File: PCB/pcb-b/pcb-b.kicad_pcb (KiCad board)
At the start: 2 copper layers, 94.7 x 42 mm, 81 parts, among them J1 Conn_02x05_Counter_Clockwise, J2 Conn_02x05_Counter_Clockwise, K1 HK19F-DCxxV-SHC, Q1 BC817, Q10 BC817, Q11 TPCA8120,L1Q, Q13 TPCA8120,L1Q, Q14 BC817, Q15 BC817, Q19 BC817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

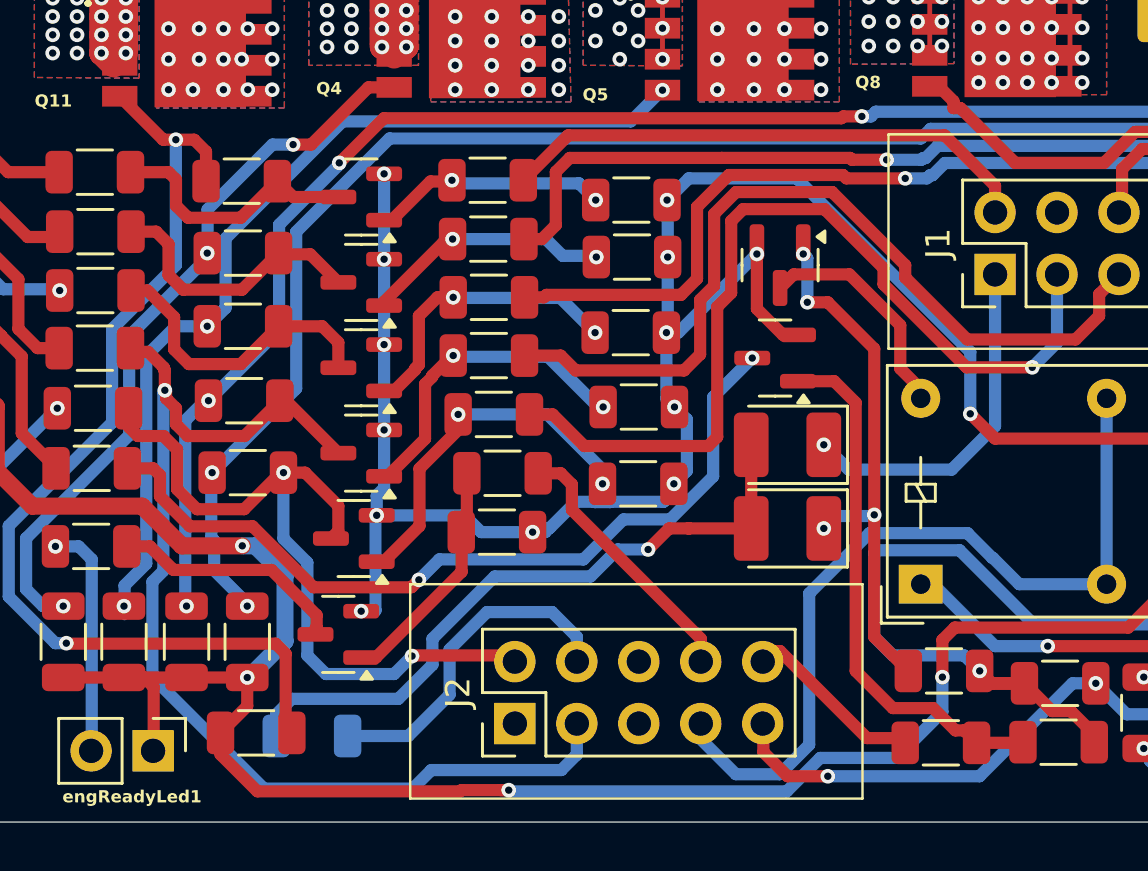
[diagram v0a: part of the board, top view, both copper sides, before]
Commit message: Small enhancement: all components on the same side
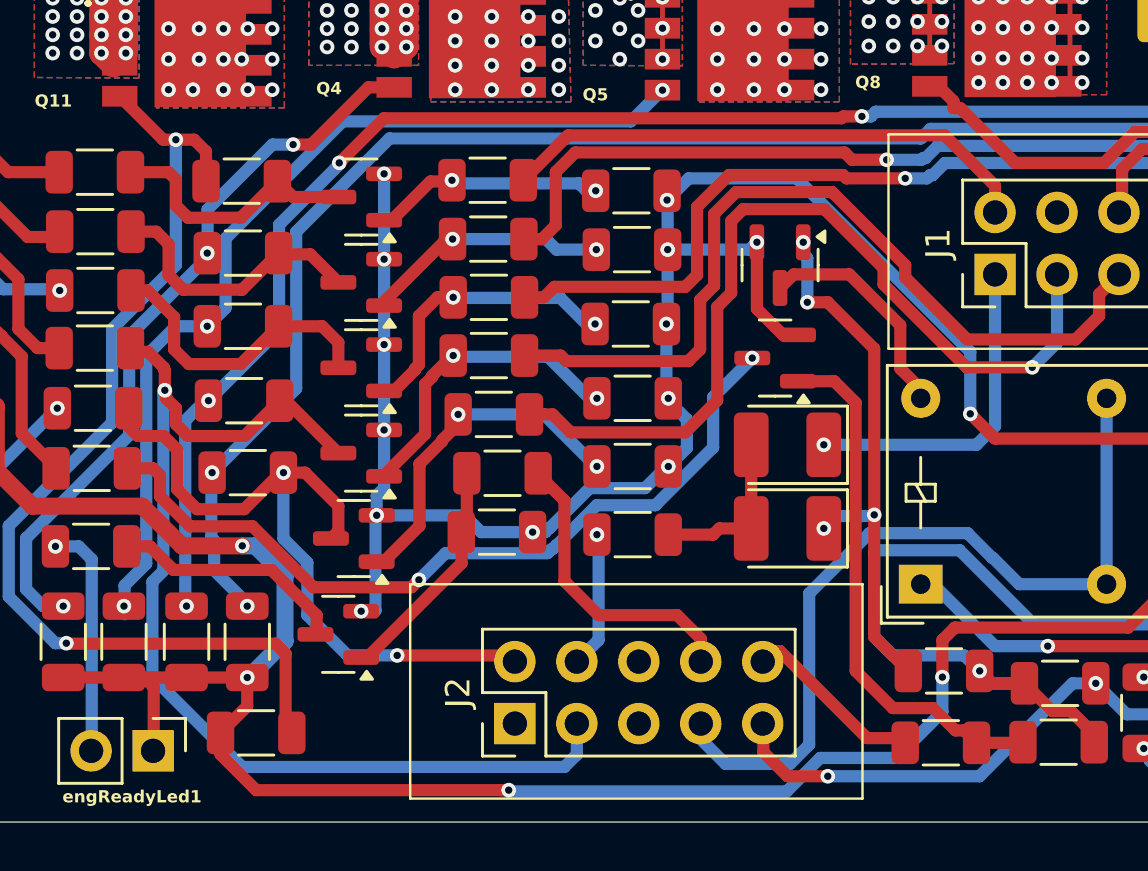
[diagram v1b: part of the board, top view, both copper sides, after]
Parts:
- RA15: moved to F.Cu
- moved RA15 15.5 mm to (137.7, 100.1), turned to 0 degrees
- moved RA38 0.75 mm to (137.7, 97.3)
- moved RA37 0.44 mm to (137.7, 94.5)
- moved RA34 0.38 mm to (137.6, 86.0)
- moved RA36 0.36 mm to (137.6, 91.5)
- moved RA35 0.30 mm to (137.7, 88.4)
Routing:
- net Net-(D2-A): track 27.6 -> 6.93 mm, vias 1 -> 0
- net o_engineON: track 14.7 -> 6.26 mm, vias 0 -> 1
- net GND: track 240.7 -> 238.8 mm
- net c_rightArrow: track 31.5 -> 29.9 mm
- net o_engineReady: track 11.0 -> 12.4 mm
- net o_rightArrow: track 37.3 -> 36.0 mm
- net Net-(Q19-B): track 15.0 -> 14.2 mm
- net i_powerOFF: track 14.4 -> 13.6 mm
- net c_leftArrow: track 45.7 -> 45.0 mm
- net Net-(Q20-C): track 33.9 -> 33.2 mm

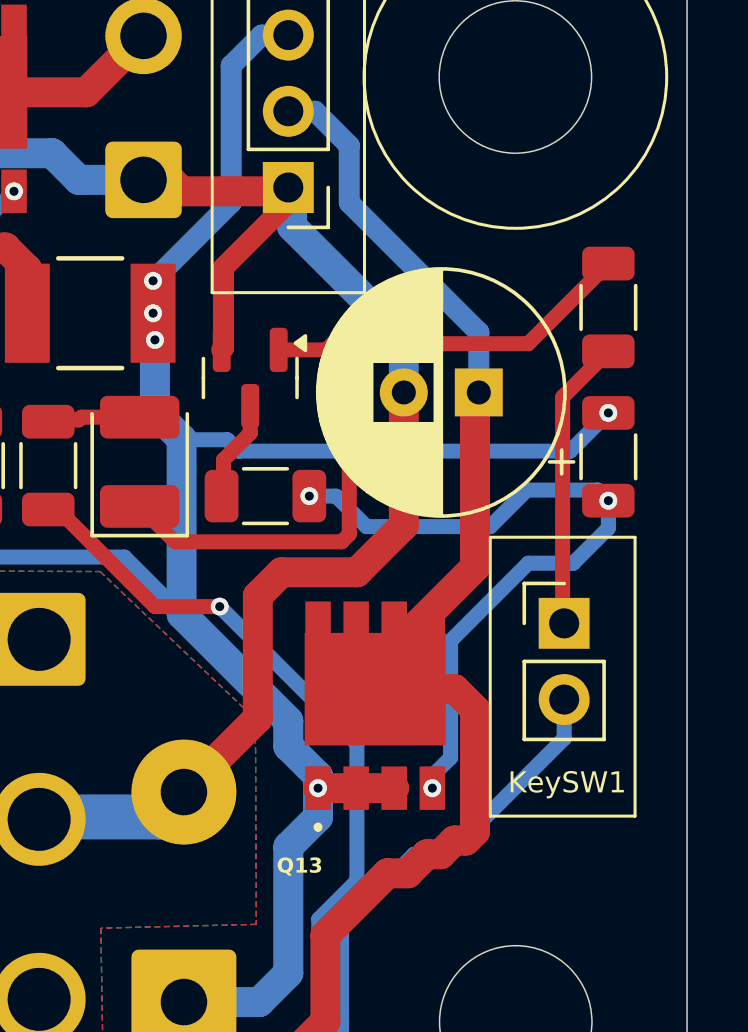
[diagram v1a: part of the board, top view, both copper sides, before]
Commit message: Floating BC817's base fixed
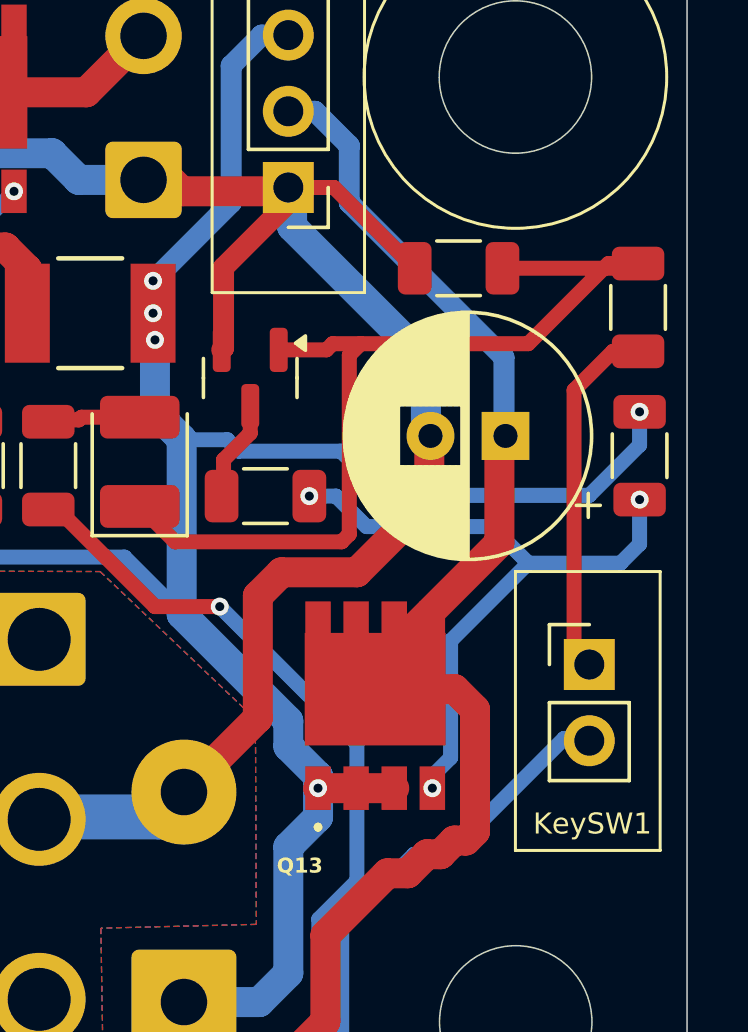
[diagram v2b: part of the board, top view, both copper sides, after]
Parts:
- added R7: 100K, Resistor_SMD:R_1206_3216Metric, F.Cu at (189.5, 81.6)
- moved C9 1.70 mm to (191.0, 87.2)
- moved KeySW1 1.61 mm to (193.8, 94.8)
- moved R2 1.04 mm to (195.5, 87.8)
- moved R4 0.99 mm to (195.4, 82.9)
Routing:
- net GND: track 238.8 -> 244.9 mm
- net Net-(D1-K): track 26.3 -> 31.7 mm
- net +12V: track 184.3 -> 187.3 mm
- net Net-(KeySW1-Pin_1): track 9.72 -> 12.0 mm
- net Net-(Q13-G): track 23.9 -> 22.5 mm
- net tempPower: track 115.9 -> 116.5 mm

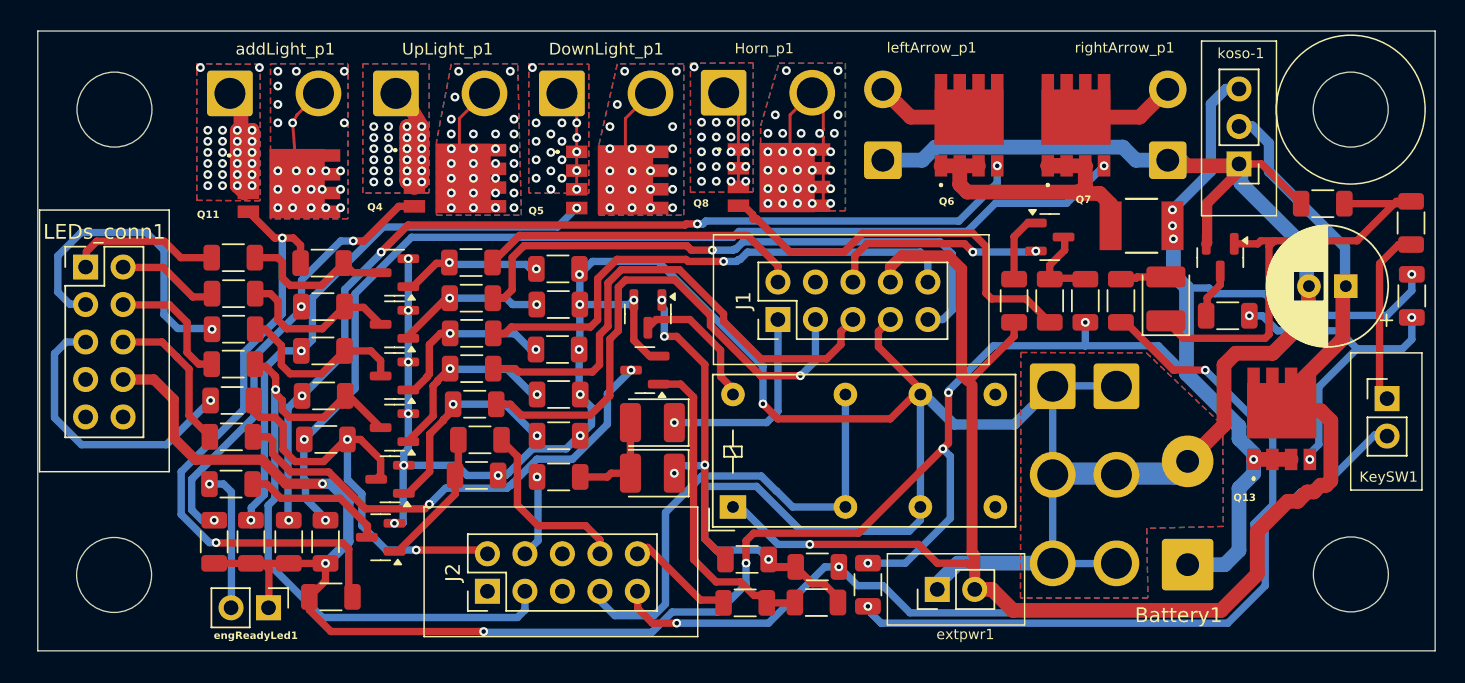
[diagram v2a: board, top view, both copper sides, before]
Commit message: Components sizes and positions optimizing
- 3-pins Koso's comnnector has been substituted with a more standard 4-pins one
- One resistor has been moved to free space for EngReady_led connector
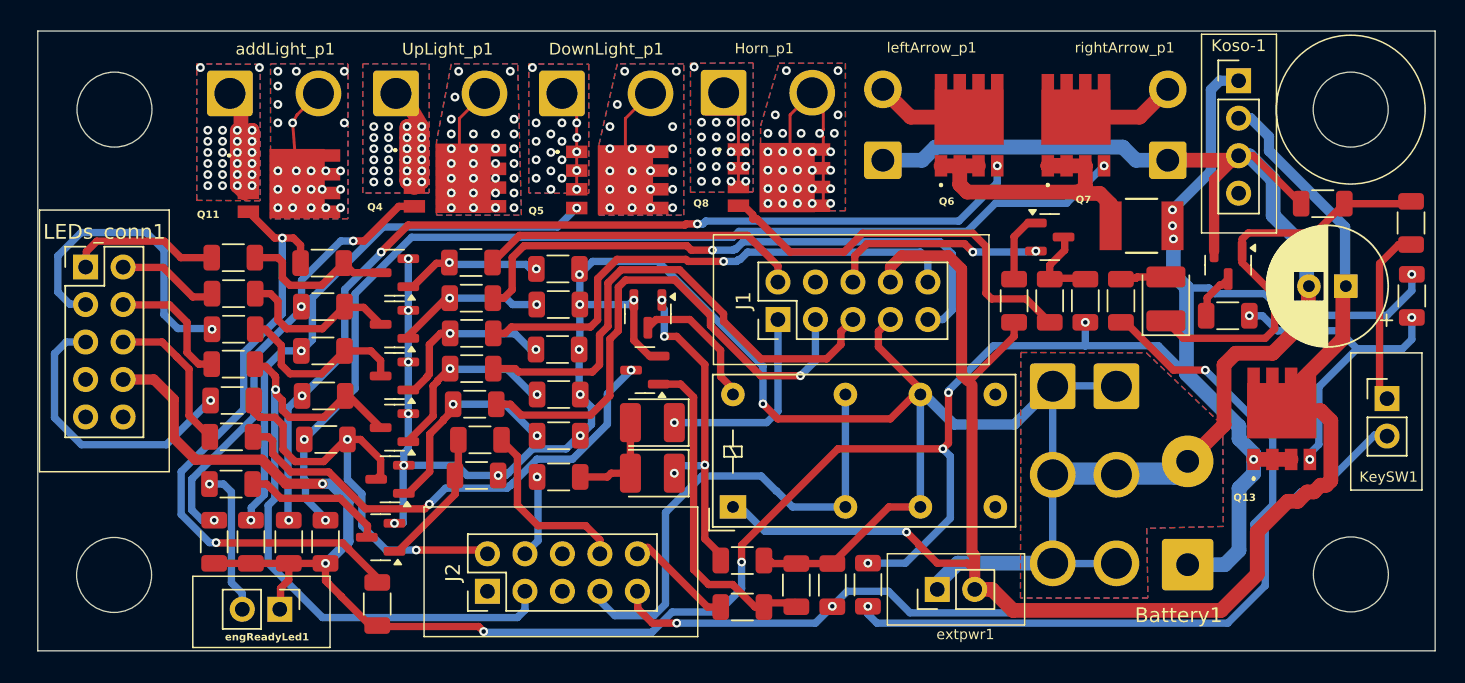
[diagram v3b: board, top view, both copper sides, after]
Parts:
- Koso-1: renamed from koso-1; value Conn_01x03 -> Conn_01x04; footprint Connector_PinHeader_2.54mm:PinHeader_1x03_P2.54mm_Vertical -> Connector_PinHeader_2.54mm:PinHeader_1x04_P2.54mm_Vertical
- moved Koso-1 5.64 mm to (183.8, 73.2), turned to 0 degrees
- moved RA24 3.18 mm to (125.4, 108.7), turned to 90 degrees
- moved RA39 1.80 mm to (153.8, 107.4), turned to 90 degrees
- moved R6 1.60 mm to (156.2, 107.4), turned to -90 degrees
- moved engReadyLed1 0.77 mm to (118.8, 109.1)
- moved Q9 0.74 mm to (183.0, 85.7)
- moved RA17 0.34 mm to (150.1, 108.9)
- moved RA8 0.33 mm to (150.1, 105.8)
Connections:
- Koso-1 pad 1: GND -> +12V
- Koso-1 pad 3: +12V -> GND
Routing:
- net GND: track 244.9 -> 226.1 mm, vias 15 -> 14
- net Net-(D1-K): track 31.7 -> 27.7 mm
- net +12V: track 187.3 -> 184.3 mm
- net o_keepAlive: track 71.7 -> 70.3 mm
- net Net-(Q20-B): track 21.8 -> 22.6 mm
- net tempPower: track 116.5 -> 117.1 mm

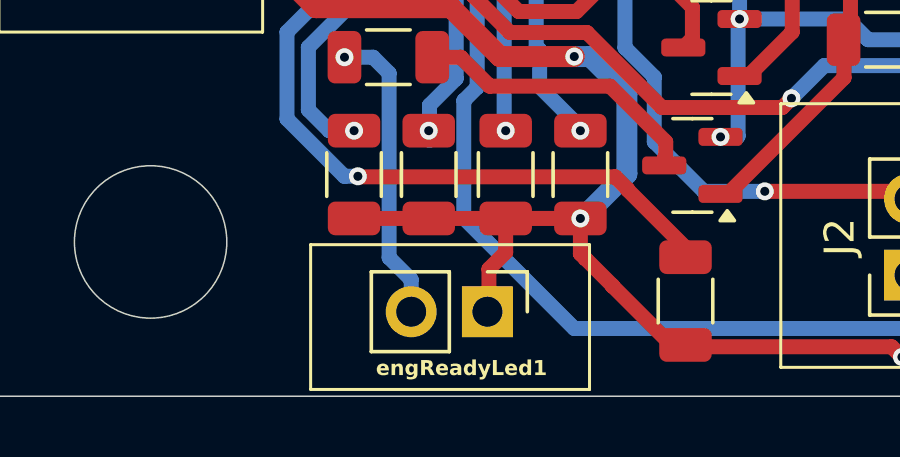
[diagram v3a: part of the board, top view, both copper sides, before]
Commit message: Wrong EngReady_LED connector orientation fixed
Standard: 1=negative 2=positive
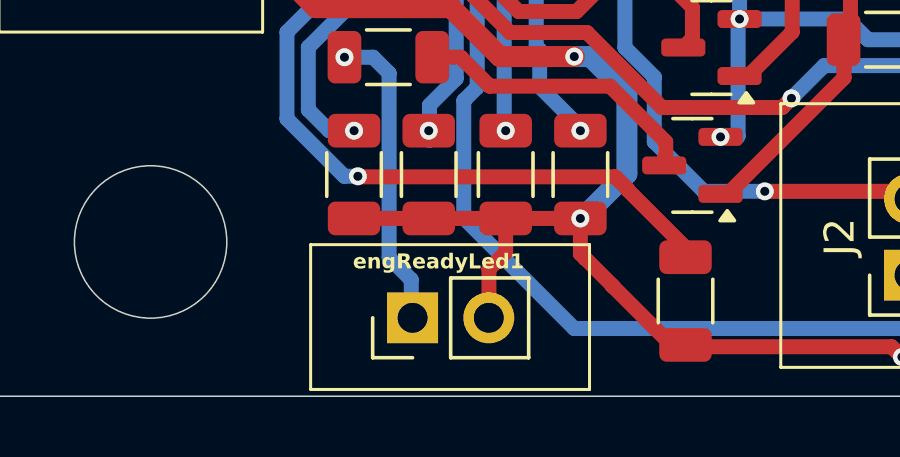
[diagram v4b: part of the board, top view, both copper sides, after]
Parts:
- moved engReadyLed1 2.50 mm to (116.3, 109.3), turned to 90 degrees
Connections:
- RA9 pad 2: Net-(engReadyLed1-Pin_2) -> Net-(engReadyLed1-Pin_1)
- engReadyLed1 pad 1: +12V -> Net-(engReadyLed1-Pin_1)
- engReadyLed1 pad 2: Net-(engReadyLed1-Pin_2) -> +12V
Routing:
- net Net-(engReadyLed1-Pin_1): track 0.00 -> 10.2 mm, vias 0 -> 1
- net Net-(engReadyLed1-Pin_2): track 9.96 -> 0.00 mm, vias 1 -> 0
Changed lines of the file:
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@@
 	(net 57 "Net-(Q20-B)")
 	(net 58 "o_neutral")
-	(net 59 "Net-(engReadyLed1-Pin_2)")
+	(net 59 "Net-(engReadyLed1-Pin_1)")
 	(net 60 "unconnected-(LEDs_conn1-Pin_7-Pad7)")
 	(net 61 "Net-(Q6-S_1)")
@@
 	(footprint "Connector_PinHeader_2.54mm:PinHeader_1x02_P2.54mm_Vertical"
 		(layer "F.Cu")
-		(at 118.7784 109.0572 -90)
+		(at 116.2842 109.2604 90)
 		(descr "Through hole straight pin header, 1x02, 2.54mm pitch, single row")
 		(tags "Through hole pin header THT 1x02 2.54mm single row")
@@
 		)
 		(property "Datasheet" "~"
-			(at 0 0 270)
+			(at 0 0 90)
 			(unlocked yes)
 			(layer "F.Fab")
@@
 		)
 		(property "Description" ""
-			(at 0 0 270)
+			(at 0 0 90)
 			(unlocked yes)
 			(layer "F.Fab")
@@
 		(attr through_hole)
 		(fp_line
-			(start -1.33 3.87)
-			(end 1.33 3.87)
+			(start -1.33 -1.33)
+			(end 0 -1.33)
 			(stroke
 				(width 0.12)
@@
 		)
 		(fp_line
-			(start -1.33 1.27)
-			(end -1.33 3.87)
+			(start -1.33 0)
+			(end -1.33 -1.33)
 			(stroke
 				(width 0.12)
@@
 		)
 		(fp_line
-			(start -1.33 1.27)
-			(end 1.33 1.27)
+			(start 1.33 1.27)
+			(end 1.33 3.87)
 			(stroke
 				(width 0.12)
@@
 		)
 		(fp_line
-			(start 1.33 1.27)
-			(end 1.33 3.87)
+			(start -1.33 1.27)
+			(end 1.33 1.27)
 			(stroke
 				(width 0.12)
@@
 		)
 		(fp_line
-			(start -1.33 0)
-			(end -1.33 -1.33)
+			(start -1.33 1.27)
+			(end -1.33 3.87)
 			(stroke
 				(width 0.12)
@@
 		)
 		(fp_line
-			(start -1.33 -1.33)
-			(end 0 -1.33)
+			(start -1.33 3.87)
+			(end 1.33 3.87)
 			(stroke
 				(width 0.12)
@@
 		)
 		(fp_line
-			(start -1.8 4.35)
-			(end 1.8 4.35)
+			(start 1.8 -1.8)
+			(end -1.8 -1.8)
 			(stroke
 				(width 0.05)
@@
 		)
 		(fp_line
-			(start 1.8 4.35)
-			(end 1.8 -1.8)
+			(start -1.8 -1.8)
+			(end -1.8 4.35)
 			(stroke
 				(width 0.05)
@@
 		)
 		(fp_line
-			(start -1.8 -1.8)
-			(end -1.8 4.35)
+			(start 1.8 4.35)
+			(end 1.8 -1.8)
 			(stroke
 				(width 0.05)
@@
 		)
 		(fp_line
-			(start 1.8 -1.8)
-			(end -1.8 -1.8)
+			(start -1.8 4.35)
+			(end 1.8 4.35)
 			(stroke
 				(width 0.05)
@@
 		)
 		(fp_line
-			(start -1.27 3.81)
-			(end -1.27 -0.635)
+			(start 1.27 -1.27)
+			(end 1.27 3.81)
 			(stroke
 				(width 0.1)
@@
 		)
 		(fp_line
-			(start 1.27 3.81)
-			(end -1.27 3.81)
+			(start -0.635 -1.27)
+			(end 1.27 -1.27)
 			(stroke
 				(width 0.1)
@@
 		)
 		(fp_line
-			(start -0.635 -1.27)
-			(end 1.27 -1.27)
+			(start 1.27 3.81)
+			(end -1.27 3.81)
 			(stroke
 				(width 0.1)
@@
 		)
 		(fp_line
-			(start 1.27 -1.27)
-			(end 1.27 3.81)
+			(start -1.27 3.81)
+			(end -1.27 -0.635)
 			(stroke
 				(width 0.1)
@@
 		)
 		(pad "1" thru_hole rect
-			(at 0 0 270)
+			(at 0 0 90)
 			(size 1.7 1.7)
 			(drill 1)
 			(layers "*.Cu" "*.Mask")
 			(remove_unused_layers no)
-			(net 22 "+12V")
+			(net 59 "Net-(engReadyLed1-Pin_1)")
 			(pinfunction "Pin_1")
 			(pintype "passive")
 		)
 		(pad "2" thru_hole oval
-			(at 0 2.54 270)
+			(at 0 2.54 90)
 			(size 1.7 1.7)
 			(drill 1)
 			(layers "*.Cu" "*.Mask")
 			(remove_unused_layers no)
-			(net 59 "Net-(engReadyLed1-Pin_2)")
+			(net 22 "+12V")
 			(pinfunction "Pin_2")
 			(pintype "passive")
@@
 			(layers "F.Cu" "F.Mask" "F.Paste")
 			(roundrect_rratio 0.222222)
-			(net 59 "Net-(engReadyLed1-Pin_2)")
+			(net 59 "Net-(engReadyLed1-Pin_1)")
 			(pintype "passive")
 		)
@@
 	)
 	(segment
-		(start 118.8292 109.0064)
-		(end 118.8292 107.6348)
-		(width 0.5)
-		(layer "F.Cu")
-		(net 22)
-	)
-	(segment
 		(start 150.0712 104.7138)
 		(end 156.599 98.186)
@@
 	)
 	(segment
+		(start 118.8292 107.6348)
+		(end 119.388 107.076)
+		(width 0.5)
+		(layer "F.Cu")
+		(net 22)
+	)
+	(segment
 		(start 124.976 110.2256)
 		(end 122.9547 108.2043)
@@
 	)
 	(segment
-		(start 156.599 98.186)
-		(end 163.711 98.186)
+		(start 118.8242 109.103)
+		(end 118.8242 109.2604)
 		(width 0.5)
 		(layer "F.Cu")
@@
 	)
 	(segment
-		(start 118.8292 107.6348)
-		(end 119.388 107.076)
+		(start 156.599 98.186)
+		(end 163.711 98.186)
 		(width 0.5)
 		(layer "F.Cu")
@@
 	)
 	(segment
-		(start 119.388 107.076)
-		(end 119.388 105.9477)
-		(width 0.5)
-		(layer "F.Cu")
-		(net 22)
-	)
-	(segment
 		(start 164.092 97.805)
 		(end 163.711 98.186)
@@
 	)
 	(segment
+		(start 119.388 107.076)
+		(end 119.388 105.9477)
+		(width 0.5)
+		(layer "F.Cu")
+		(net 22)
+	)
+	(segment
 		(start 132.596 110.5662)
 		(end 132.2554 110.2256)
@@
 	)
 	(segment
+		(start 118.8292 109.2554)
+		(end 118.8292 107.6348)
+		(width 0.5)
+		(layer "F.Cu")
+		(net 22)
+	)
+	(segment
 		(start 119.19765 100.5516)
 		(end 117.56865 98.9226)
@@
 	)
 	(segment
+		(start 118.8242 109.2604)
+		(end 118.8292 109.2554)
+		(width 0.5)
+		(layer "F.Cu")
+		(net 22)
+	)
+	(segment
 		(start 122.9547 108.2043)
 		(end 122.944 108.2043)
@@
 	(segment
 		(start 118.7784 109.0572)
-		(end 118.8292 109.0064)
+		(end 118.8242 109.103)
 		(width 0.5)
 		(layer "F.Cu")
@@
 	)
 	(segment
+		(start 115.5018 107.2538)
+		(end 116.2384 107.9904)
+		(width 0.5)
+		(layer "B.Cu")
+		(net 59)
+	)
+	(segment
+		(start 116.2384 109.2146)
+		(end 116.2842 109.2604)
+		(width 0.5)
+		(layer "B.Cu")
+		(net 59)
+	)
+	(segment
 		(start 115.5018 101.107)
 		(end 115.5018 107.2538)
@@
 	)
 	(segment
-		(start 115.5018 107.2538)
-		(end 116.2384 107.9904)
-		(width 0.5)
-		(layer "B.Cu")
-		(net 59)
-	)
-	(segment
 		(start 116.2384 107.9904)
-		(end 116.2384 109.0572)
+		(end 116.2384 109.2146)
 		(width 0.5)
 		(layer "B.Cu")
